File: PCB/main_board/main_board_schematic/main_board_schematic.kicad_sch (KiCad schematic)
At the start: 257 parts, among them J1 Conn_01x02, P1 USB_C_Plug_USB2.0, SW1 tactile_switch, SW10 SW_MEC_5G, SW100 SW_MEC_5G, SW101 SW_MEC_5G, SW102 SW_MEC_5G, SW103 SW_MEC_5G, SW104 SW_MEC_5G, SW105 SW_MEC_5G, SW106 SW_MEC_5G, SW107 SW_MEC_5G, SW108 SW_MEC_5G, SW109 SW_MEC_5G, SW11 SW_MEC_5G, SW110 SW_MEC_5G, SW12 SW_MEC_5G, SW13 SW_MEC_5G, SW14 SW_MEC_5G, SW15 SW_MEC_5G, SW16 SW_MEC_5G, SW17 SW_MEC_5G, SW18 SW_MEC_5G, SW19 SW_MEC_5G, SW2 SW_MEC_5G, SW20 SW_MEC_5G, SW21 SW_MEC_5G, SW22 SW_MEC_5G, SW23 SW_MEC_5G, SW24 SW_MEC_5G, SW25 SW_MEC_5G, SW26 SW_MEC_5G, SW27 SW_MEC_5G, SW28 SW_MEC_5G, SW29 SW_MEC_5G, SW3 SW_MEC_5G, SW30 SW_MEC_5G, SW31 SW_MEC_5G, SW32 SW_MEC_5G, SW33 SW_MEC_5G, SW34 SW_MEC_5G, SW35 SW_MEC_5G, SW36 SW_MEC_5G, SW37 SW_MEC_5G, SW38 SW_MEC_5G, SW39 SW_MEC_5G, SW4 SW_MEC_5G, SW40 SW_MEC_5G, SW41 SW_MEC_5G, SW42 SW_MEC_5G, SW43 SW_MEC_5G, SW44 SW_MEC_5G, SW45 SW_MEC_5G, SW46 SW_MEC_5G, SW47 SW_MEC_5G, SW48 SW_MEC_5G, SW49 SW_MEC_5G, SW5 SW_MEC_5G, SW50 SW_MEC_5G, SW51 SW_MEC_5G, SW52 SW_MEC_5G, SW53 SW_MEC_5G, SW54 SW_MEC_5G, SW55 SW_MEC_5G, SW56 SW_MEC_5G, SW57 SW_MEC_5G, SW58 SW_MEC_5G, SW59 SW_MEC_5G, SW6 SW_MEC_5G, SW60 SW_MEC_5G, SW61 SW_MEC_5G, SW62 SW_MEC_5G, SW63 SW_MEC_5G, SW64 SW_MEC_5G, SW65 SW_MEC_5G, SW66 SW_MEC_5G, SW67 SW_MEC_5G, SW68 SW_MEC_5G, SW69 SW_MEC_5G, SW7 SW_MEC_5G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

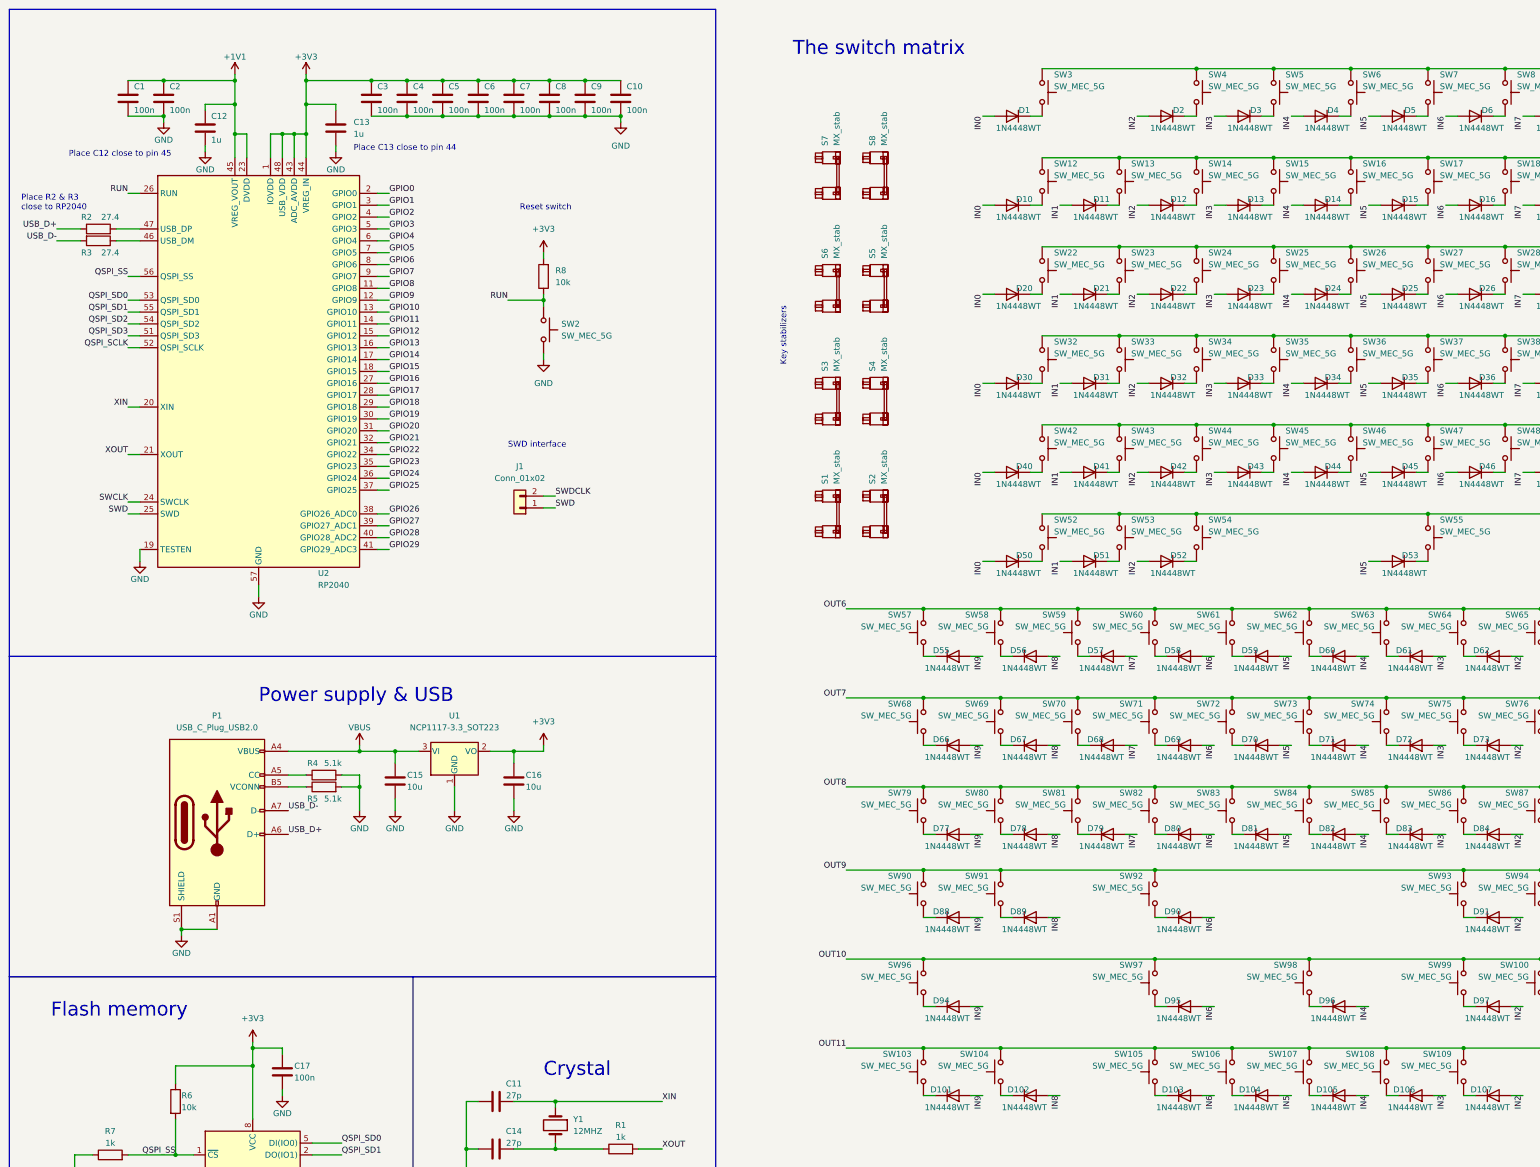
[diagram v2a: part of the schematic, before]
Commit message: Added labels to the stabilizers
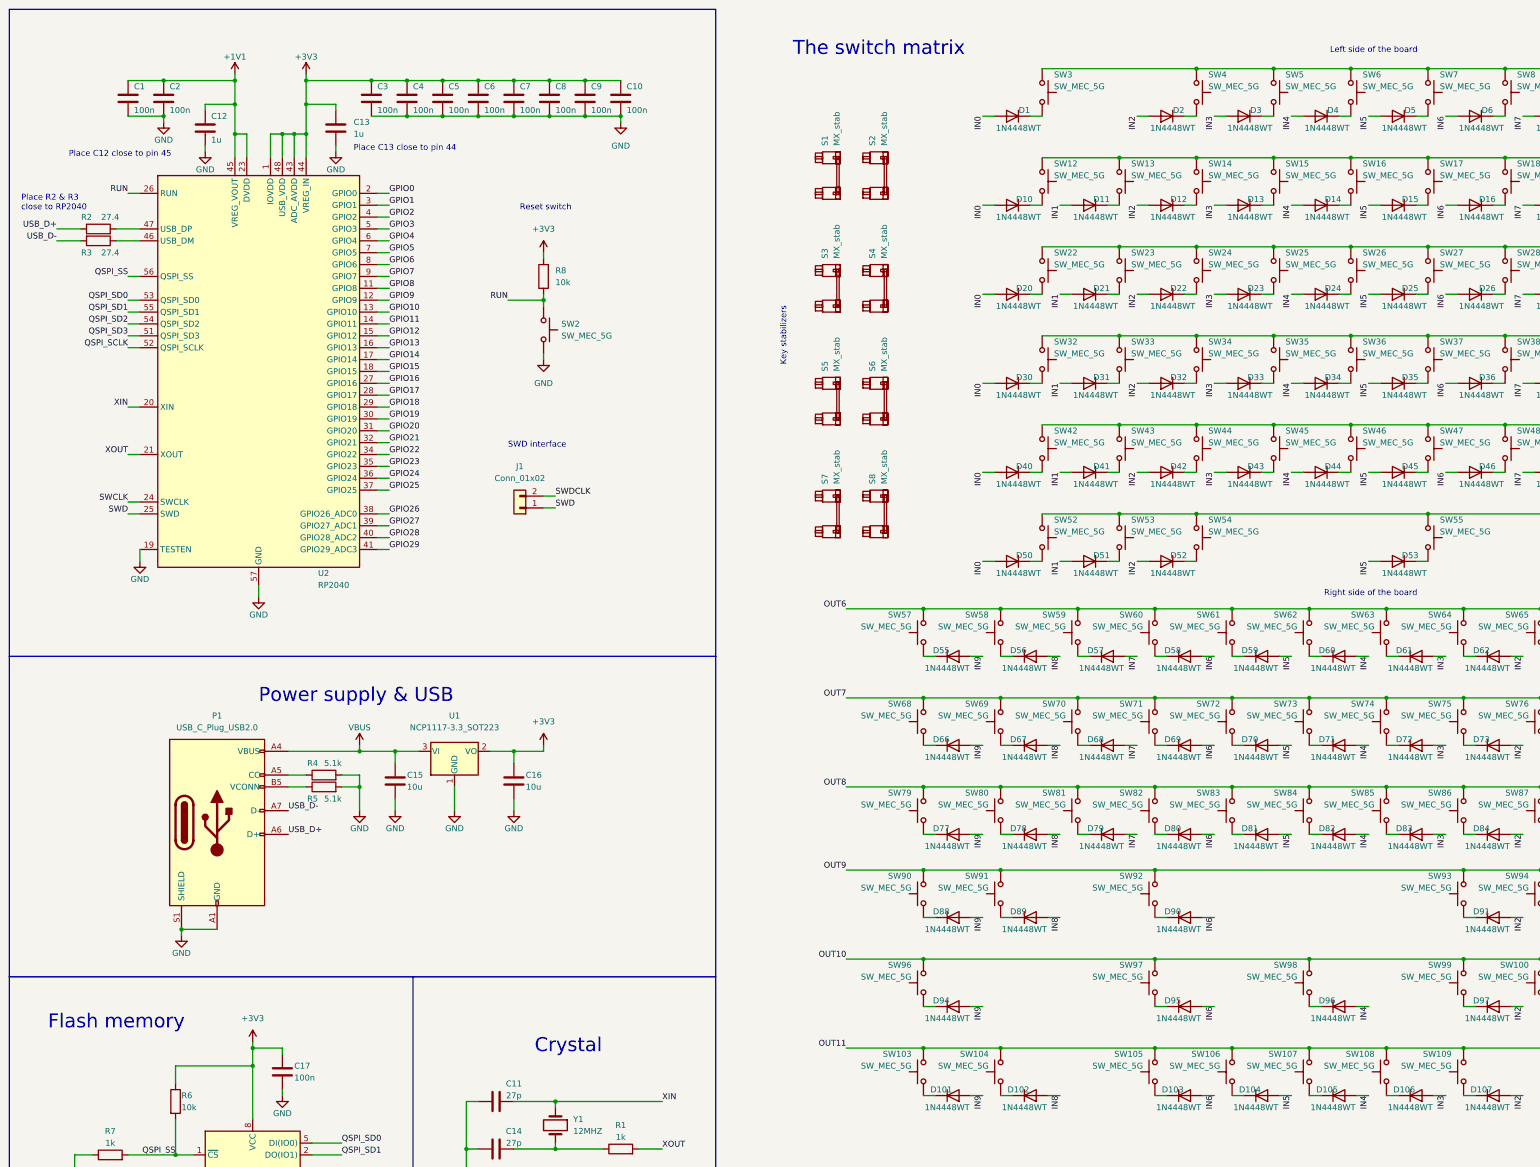
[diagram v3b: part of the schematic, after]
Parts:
- renumbered S7 to S1, S8 to S2, S6 to S3, S5 to S4, S3 to S5, S4 to S6, S1 to S7, S2 to S8
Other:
- note added: "Left side of the board"
- note added: "Right side of the board"
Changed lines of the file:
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@@
     (effects (font (size 1.27 1.27)) (justify left bottom))
   )
-  (text "Crystal" (at 128.27 242.57 0)
+  (text "Crystal" (at 126.365 237.49 0)
     (effects (font (size 3 3)) (justify left bottom))
   )
+  (text "Right side of the board" (at 295.275 139.7 0)
+    (effects (font (size 1.27 1.27)) (justify left bottom))
+  )
   (text "Key stabilizers\n" (at 180.34 90.17 90)
     (effects (font (size 1.27 1.27)) (justify left bottom))
@@
     (effects (font (size 2 2)) (justify left bottom))
   )
+  (text "Left side of the board" (at 296.545 23.495 0)
+    (effects (font (size 1.27 1.27)) (justify left bottom))
+  )
   (text "Reset switch" (at 123.19 57.15 0)
     (effects (font (size 1.27 1.27)) (justify left bottom))
@@
     (effects (font (size 1.27 1.27)) (justify left bottom))
   )
-  (text "Flash memory\n" (at 22.86 229.87 0)
+  (text "Flash memory\n" (at 22.225 232.41 0)
     (effects (font (size 3 3)) (justify left bottom))
   )
@@
   (symbol (lib_id "PCM_marbastlib-mx:MX_stab") (at 189.23 73.66 90) (unit 1)
     (in_bom yes) (on_board yes) (dnp no) (fields_autoplaced)
-    (property "Reference" "S6" (at 188.468 67.31 0)
+    (property "Reference" "S3" (at 188.468 67.31 0)
       (effects (font (size 1.27 1.27)) (justify left))
     )
@@
       (project "main_board_schematic"
         (path "/eeca1343-c7ac-4fd3-9bdf-4d43c95df1aa"
-          (reference "S6") (unit 1)
+          (reference "S3") (unit 1)
         )
       )
@@
   (symbol (lib_id "PCM_marbastlib-mx:MX_stab") (at 189.23 49.53 90) (unit 1)
     (in_bom yes) (on_board yes) (dnp no) (fields_autoplaced)
-    (property "Reference" "S7" (at 188.468 43.18 0)
+    (property "Reference" "S1" (at 188.468 43.18 0)
       (effects (font (size 1.27 1.27)) (justify left))
     )
@@
       (project "main_board_schematic"
         (path "/eeca1343-c7ac-4fd3-9bdf-4d43c95df1aa"
-          (reference "S7") (unit 1)
+          (reference "S1") (unit 1)
         )
       )
@@
   (symbol (lib_id "PCM_marbastlib-mx:MX_stab") (at 199.39 121.92 90) (unit 1)
     (in_bom yes) (on_board yes) (dnp no) (fields_autoplaced)
-    (property "Reference" "S2" (at 198.628 115.57 0)
+    (property "Reference" "S8" (at 198.628 115.57 0)
       (effects (font (size 1.27 1.27)) (justify left))
     )
@@
       (project "main_board_schematic"
         (path "/eeca1343-c7ac-4fd3-9bdf-4d43c95df1aa"
-          (reference "S2") (unit 1)
+          (reference "S8") (unit 1)
         )
       )
@@
   (symbol (lib_id "PCM_marbastlib-mx:MX_stab") (at 189.23 121.92 90) (unit 1)
     (in_bom yes) (on_board yes) (dnp no) (fields_autoplaced)
-    (property "Reference" "S1" (at 188.468 115.57 0)
+    (property "Reference" "S7" (at 188.468 115.57 0)
       (effects (font (size 1.27 1.27)) (justify left))
     )
@@
       (project "main_board_schematic"
         (path "/eeca1343-c7ac-4fd3-9bdf-4d43c95df1aa"
-          (reference "S1") (unit 1)
+          (reference "S7") (unit 1)
         )
       )
@@
   (symbol (lib_id "PCM_marbastlib-mx:MX_stab") (at 199.39 73.66 90) (unit 1)
     (in_bom yes) (on_board yes) (dnp no) (fields_autoplaced)
-    (property "Reference" "S5" (at 198.628 67.31 0)
+    (property "Reference" "S4" (at 198.628 67.31 0)
       (effects (font (size 1.27 1.27)) (justify left))
     )
@@
       (project "main_board_schematic"
         (path "/eeca1343-c7ac-4fd3-9bdf-4d43c95df1aa"
-          (reference "S5") (unit 1)
+          (reference "S4") (unit 1)
         )
       )
@@
   (symbol (lib_id "PCM_marbastlib-mx:MX_stab") (at 199.39 97.79 90) (unit 1)
     (in_bom yes) (on_board yes) (dnp no) (fields_autoplaced)
-    (property "Reference" "S4" (at 198.628 91.44 0)
+    (property "Reference" "S6" (at 198.628 91.44 0)
       (effects (font (size 1.27 1.27)) (justify left))
     )
@@
       (project "main_board_schematic"
         (path "/eeca1343-c7ac-4fd3-9bdf-4d43c95df1aa"
-          (reference "S4") (unit 1)
+          (reference "S6") (unit 1)
         )
       )
@@
   (symbol (lib_id "PCM_marbastlib-mx:MX_stab") (at 189.23 97.79 90) (unit 1)
     (in_bom yes) (on_board yes) (dnp no) (fields_autoplaced)
-    (property "Reference" "S3" (at 188.468 91.44 0)
+    (property "Reference" "S5" (at 188.468 91.44 0)
       (effects (font (size 1.27 1.27)) (justify left))
     )
@@
       (project "main_board_schematic"
         (path "/eeca1343-c7ac-4fd3-9bdf-4d43c95df1aa"
-          (reference "S3") (unit 1)
+          (reference "S5") (unit 1)
         )
       )
@@
   (symbol (lib_id "PCM_marbastlib-mx:MX_stab") (at 199.39 49.53 90) (unit 1)
     (in_bom yes) (on_board yes) (dnp no) (fields_autoplaced)
-    (property "Reference" "S8" (at 198.628 43.18 0)
+    (property "Reference" "S2" (at 198.628 43.18 0)
       (effects (font (size 1.27 1.27)) (justify left))
     )
@@
       (project "main_board_schematic"
         (path "/eeca1343-c7ac-4fd3-9bdf-4d43c95df1aa"
-          (reference "S8") (unit 1)
+          (reference "S2") (unit 1)
         )
       )

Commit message: Added footprints for all components
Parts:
- removed SW1: tactile_switch, symbol Switch:SW_MEC_5G
- removed SW2: SW_MEC_5G, symbol Switch:SW_MEC_5G
- added J2, J3: Conn_01x02, Connector_PinHeader_2.54mm:PinHeader_1x02_P2.54mm_Horizontal, symbol Connector_Generic:Conn_01x02
- C1, C10, C11, C12, C13, C14, C15, C16, C17, C2, C3, C4, C5, C6, C7, C8, C9: footprint (none) -> Capacitor_SMD:C_0603_1608Metric
- J1: footprint (none) -> Connector_PinHeader_2.54mm:PinHeader_1x02_P2.54mm_Horizontal
- P1: footprint (none) -> Connector_USB:USB_C_Receptacle_GCT_USB4135-GF-A_6P_TopMnt_Horizontal
- R1, R2, R3, R4, R5, R6, R7, R8: footprint (none) -> Resistor_SMD:R_0603_1608Metric
- S2, S3, S4, S5, S6, S7, S8: footprint PCM_marbastlib-mx:STAB_MX_P_6.25u -> PCM_marbastlib-mx:STAB_MX_2u
- SW1: renamed from SW3; footprint (none) -> Button_Switch_Keyboard:SW_Cherry_MX_1.00u_PCB
- SW10: renamed from SW12; footprint (none) -> Button_Switch_Keyboard:SW_Cherry_MX_1.00u_PCB
- SW100: renamed from SW102; footprint (none) -> Button_Switch_Keyboard:SW_Cherry_MX_2.00u_Vertical_PCB
- SW101: renamed from SW103; footprint (none) -> Button_Switch_Keyboard:SW_Cherry_MX_1.25u_PCB
- SW102: renamed from SW104; footprint (none) -> Button_Switch_Keyboard:SW_Cherry_MX_1.25u_PCB
- SW103: renamed from SW105; footprint (none) -> Button_Switch_Keyboard:SW_Cherry_MX_1.25u_PCB
- SW104: renamed from SW106; footprint (none) -> Button_Switch_Keyboard:SW_Cherry_MX_1.00u_PCB
- SW105: renamed from SW107; footprint (none) -> Button_Switch_Keyboard:SW_Cherry_MX_1.00u_PCB
- SW106: renamed from SW108; footprint (none) -> Button_Switch_Keyboard:SW_Cherry_MX_1.00u_PCB
- SW107: renamed from SW109; footprint (none) -> Button_Switch_Keyboard:SW_Cherry_MX_2.00u_PCB
- SW108: renamed from SW110; footprint (none) -> Button_Switch_Keyboard:SW_Cherry_MX_1.00u_PCB
- SW11: renamed from SW13; footprint (none) -> Button_Switch_Keyboard:SW_Cherry_MX_1.00u_PCB
- SW12: renamed from SW14; footprint (none) -> Button_Switch_Keyboard:SW_Cherry_MX_1.00u_PCB
- SW13: renamed from SW15; footprint (none) -> Button_Switch_Keyboard:SW_Cherry_MX_1.00u_PCB
- SW14: renamed from SW16; footprint (none) -> Button_Switch_Keyboard:SW_Cherry_MX_1.00u_PCB
- SW15: renamed from SW17; footprint (none) -> Button_Switch_Keyboard:SW_Cherry_MX_1.00u_PCB
- SW16: renamed from SW18; footprint (none) -> Button_Switch_Keyboard:SW_Cherry_MX_1.00u_PCB
- SW17: renamed from SW19; footprint (none) -> Button_Switch_Keyboard:SW_Cherry_MX_1.00u_PCB
- SW18: renamed from SW20; footprint (none) -> Button_Switch_Keyboard:SW_Cherry_MX_1.00u_PCB
- SW19: renamed from SW21; footprint (none) -> Button_Switch_Keyboard:SW_Cherry_MX_1.00u_PCB
- SW2: renamed from SW4; footprint (none) -> Button_Switch_Keyboard:SW_Cherry_MX_1.00u_PCB
- SW20: renamed from SW22; footprint (none) -> Button_Switch_Keyboard:SW_Cherry_MX_1.50u_PCB
- SW21: renamed from SW23; footprint (none) -> Button_Switch_Keyboard:SW_Cherry_MX_1.00u_PCB
- SW22: renamed from SW24; footprint (none) -> Button_Switch_Keyboard:SW_Cherry_MX_1.00u_PCB
- SW23: renamed from SW25; footprint (none) -> Button_Switch_Keyboard:SW_Cherry_MX_1.00u_PCB
- SW24: renamed from SW26; footprint (none) -> Button_Switch_Keyboard:SW_Cherry_MX_1.00u_PCB
- SW25: renamed from SW27; footprint (none) -> Button_Switch_Keyboard:SW_Cherry_MX_1.00u_PCB
- SW26: renamed from SW28; footprint (none) -> Button_Switch_Keyboard:SW_Cherry_MX_1.00u_PCB
- SW27: renamed from SW29; footprint (none) -> Button_Switch_Keyboard:SW_Cherry_MX_1.00u_PCB
- SW28: renamed from SW30; footprint (none) -> Button_Switch_Keyboard:SW_Cherry_MX_1.00u_PCB
- SW29: renamed from SW31; footprint (none) -> Button_Switch_Keyboard:SW_Cherry_MX_1.00u_PCB
- SW3: renamed from SW5; footprint (none) -> Button_Switch_Keyboard:SW_Cherry_MX_1.00u_PCB
- SW30: renamed from SW32; footprint (none) -> Button_Switch_Keyboard:SW_Cherry_MX_1.75u_PCB
- SW31: renamed from SW33; footprint (none) -> Button_Switch_Keyboard:SW_Cherry_MX_1.00u_PCB
- SW32: renamed from SW34; footprint (none) -> Button_Switch_Keyboard:SW_Cherry_MX_1.00u_PCB
- SW33: renamed from SW35; footprint (none) -> Button_Switch_Keyboard:SW_Cherry_MX_1.00u_PCB
- SW34: renamed from SW36; footprint (none) -> Button_Switch_Keyboard:SW_Cherry_MX_1.00u_PCB
- SW35: renamed from SW37; footprint (none) -> Button_Switch_Keyboard:SW_Cherry_MX_1.00u_PCB
- SW36: renamed from SW38; footprint (none) -> Button_Switch_Keyboard:SW_Cherry_MX_1.00u_PCB
- SW37: renamed from SW39; footprint (none) -> Button_Switch_Keyboard:SW_Cherry_MX_1.00u_PCB
- SW38: renamed from SW40; footprint (none) -> Button_Switch_Keyboard:SW_Cherry_MX_1.00u_PCB
- SW39: renamed from SW41; footprint (none) -> Button_Switch_Keyboard:SW_Cherry_MX_1.00u_PCB
- SW4: renamed from SW6; footprint (none) -> Button_Switch_Keyboard:SW_Cherry_MX_1.00u_PCB
- SW40: renamed from SW42; footprint (none) -> Button_Switch_Keyboard:SW_Cherry_MX_2.25u_PCB
- SW41: renamed from SW43; footprint (none) -> Button_Switch_Keyboard:SW_Cherry_MX_1.00u_PCB
- SW42: renamed from SW44; footprint (none) -> Button_Switch_Keyboard:SW_Cherry_MX_1.00u_PCB
- SW43: renamed from SW45; footprint (none) -> Button_Switch_Keyboard:SW_Cherry_MX_1.00u_PCB
- SW44: renamed from SW46; footprint (none) -> Button_Switch_Keyboard:SW_Cherry_MX_1.00u_PCB
- SW45: renamed from SW47; footprint (none) -> Button_Switch_Keyboard:SW_Cherry_MX_1.00u_PCB
- SW46: renamed from SW48; footprint (none) -> Button_Switch_Keyboard:SW_Cherry_MX_1.00u_PCB
- SW47: renamed from SW49; footprint (none) -> Button_Switch_Keyboard:SW_Cherry_MX_1.00u_PCB
- SW48: renamed from SW50; footprint (none) -> Button_Switch_Keyboard:SW_Cherry_MX_1.00u_PCB
- SW49: renamed from SW51; footprint (none) -> Button_Switch_Keyboard:SW_Cherry_MX_1.00u_PCB
- SW5: renamed from SW7; footprint (none) -> Button_Switch_Keyboard:SW_Cherry_MX_1.00u_PCB
- SW50: renamed from SW52; footprint (none) -> Button_Switch_Keyboard:SW_Cherry_MX_1.25u_PCB
- SW51: renamed from SW53; footprint (none) -> Button_Switch_Keyboard:SW_Cherry_MX_1.25u_PCB
- SW52: renamed from SW54; footprint (none) -> Button_Switch_Keyboard:SW_Cherry_MX_1.25u_PCB
- SW53: renamed from SW55; footprint (none) -> Button_Switch_Keyboard:SW_Cherry_MX_6.25u_PCB
- SW54: renamed from SW56; footprint (none) -> Button_Switch_Keyboard:SW_Cherry_MX_1.25u_PCB
- SW55: renamed from SW57; footprint (none) -> Button_Switch_Keyboard:SW_Cherry_MX_1.00u_PCB
- SW56: renamed from SW58; footprint (none) -> Button_Switch_Keyboard:SW_Cherry_MX_1.00u_PCB
- SW57: renamed from SW59; footprint (none) -> Button_Switch_Keyboard:SW_Cherry_MX_1.00u_PCB
- SW58: renamed from SW60; footprint (none) -> Button_Switch_Keyboard:SW_Cherry_MX_1.00u_PCB
- SW59: renamed from SW61; footprint (none) -> Button_Switch_Keyboard:SW_Cherry_MX_1.00u_PCB
- SW6: renamed from SW8; footprint (none) -> Button_Switch_Keyboard:SW_Cherry_MX_1.00u_PCB
- SW60: renamed from SW62; footprint (none) -> Button_Switch_Keyboard:SW_Cherry_MX_1.00u_PCB
- SW61: renamed from SW63; footprint (none) -> Button_Switch_Keyboard:SW_Cherry_MX_1.00u_PCB
- SW62: renamed from SW64; footprint (none) -> Button_Switch_Keyboard:SW_Cherry_MX_1.00u_PCB
- SW63: renamed from SW65; footprint (none) -> Button_Switch_Keyboard:SW_Cherry_MX_1.00u_PCB
- SW64: renamed from SW66; footprint (none) -> Button_Switch_Keyboard:SW_Cherry_MX_1.00u_PCB
- SW65: renamed from SW67; footprint (none) -> Button_Switch_Keyboard:SW_Cherry_MX_1.00u_PCB
- SW66: renamed from SW68; footprint (none) -> Button_Switch_Keyboard:SW_Cherry_MX_1.00u_PCB
- SW67: renamed from SW69; footprint (none) -> Button_Switch_Keyboard:SW_Cherry_MX_1.00u_PCB
- SW68: renamed from SW70; footprint (none) -> Button_Switch_Keyboard:SW_Cherry_MX_1.00u_PCB
- SW69: renamed from SW71; footprint (none) -> Button_Switch_Keyboard:SW_Cherry_MX_2.00u_PCB
- SW7: renamed from SW9; footprint (none) -> Button_Switch_Keyboard:SW_Cherry_MX_1.00u_PCB
- SW70: renamed from SW72; footprint (none) -> Button_Switch_Keyboard:SW_Cherry_MX_1.00u_PCB
- SW71: renamed from SW73; footprint (none) -> Button_Switch_Keyboard:SW_Cherry_MX_1.00u_PCB
- SW72: renamed from SW74; footprint (none) -> Button_Switch_Keyboard:SW_Cherry_MX_1.00u_PCB
- SW73: renamed from SW75; footprint (none) -> Button_Switch_Keyboard:SW_Cherry_MX_1.00u_PCB
- SW74: renamed from SW76; footprint (none) -> Button_Switch_Keyboard:SW_Cherry_MX_1.00u_PCB
- SW75: renamed from SW77; footprint (none) -> Button_Switch_Keyboard:SW_Cherry_MX_1.00u_PCB
- SW76: renamed from SW78; footprint (none) -> Button_Switch_Keyboard:SW_Cherry_MX_1.00u_PCB
- SW77: renamed from SW79; footprint (none) -> Button_Switch_Keyboard:SW_Cherry_MX_1.00u_PCB
- SW78: renamed from SW80; footprint (none) -> Button_Switch_Keyboard:SW_Cherry_MX_1.00u_PCB
- SW79: renamed from SW81; footprint (none) -> Button_Switch_Keyboard:SW_Cherry_MX_1.00u_PCB
- SW8: renamed from SW10; footprint (none) -> Button_Switch_Keyboard:SW_Cherry_MX_1.00u_PCB
- SW80: renamed from SW82; footprint (none) -> Button_Switch_Keyboard:SW_Cherry_MX_1.50u_PCB
- SW81: renamed from SW83; footprint (none) -> Button_Switch_Keyboard:SW_Cherry_MX_1.00u_PCB
- SW82: renamed from SW84; footprint (none) -> Button_Switch_Keyboard:SW_Cherry_MX_1.00u_PCB
- SW83: renamed from SW85; footprint (none) -> Button_Switch_Keyboard:SW_Cherry_MX_1.00u_PCB
- SW84: renamed from SW86; footprint (none) -> Button_Switch_Keyboard:SW_Cherry_MX_1.00u_PCB
- SW85: renamed from SW87; footprint (none) -> Button_Switch_Keyboard:SW_Cherry_MX_1.00u_PCB
- SW86: renamed from SW88; footprint (none) -> Button_Switch_Keyboard:SW_Cherry_MX_1.00u_PCB
- SW87: renamed from SW89; footprint (none) -> Button_Switch_Keyboard:SW_Cherry_MX_2.00u_Vertical_PCB
- SW88: renamed from SW90; footprint (none) -> Button_Switch_Keyboard:SW_Cherry_MX_1.00u_PCB
- SW89: renamed from SW91; footprint (none) -> Button_Switch_Keyboard:SW_Cherry_MX_1.00u_PCB
- SW9: renamed from SW11; footprint (none) -> Button_Switch_Keyboard:SW_Cherry_MX_1.00u_PCB
- SW90: renamed from SW92; footprint (none) -> Button_Switch_Keyboard:SW_Cherry_MX_2.25u_PCB
- SW91: renamed from SW93; footprint (none) -> Button_Switch_Keyboard:SW_Cherry_MX_1.00u_PCB
- SW92: renamed from SW94; footprint (none) -> Button_Switch_Keyboard:SW_Cherry_MX_1.00u_PCB
- SW93: renamed from SW95; footprint (none) -> Button_Switch_Keyboard:SW_Cherry_MX_1.00u_PCB
- SW94: renamed from SW96; footprint (none) -> Button_Switch_Keyboard:SW_Cherry_MX_1.00u_PCB
- SW95: renamed from SW97; footprint (none) -> Button_Switch_Keyboard:SW_Cherry_MX_2.75u_PCB
- SW96: renamed from SW98; footprint (none) -> Button_Switch_Keyboard:SW_Cherry_MX_1.00u_PCB
- SW97: renamed from SW99; footprint (none) -> Button_Switch_Keyboard:SW_Cherry_MX_1.00u_PCB
- SW98: renamed from SW100; footprint (none) -> Button_Switch_Keyboard:SW_Cherry_MX_1.00u_PCB
- SW99: renamed from SW101; footprint (none) -> Button_Switch_Keyboard:SW_Cherry_MX_1.00u_PCB
- Y1: footprint (none) -> Crystal:Crystal_HC49-U_Vertical
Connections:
- net GND: now also J2.1 (Pin_1), J3.2 (Pin_2)
- net RUN: now also J3.1 (Pin_1)
- net at R7.1: now also J2.2 (Pin_2)
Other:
- note added: "Reset connector"
- note added: "USB boot connector"
- note removed: "Reset switch"
- note removed: "USB boot switch"
